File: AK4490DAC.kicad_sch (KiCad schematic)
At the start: 77 parts, among them IC1 LP5907MFX-3.3/NOPB, IC2 LP5907MFX-3.3/NOPB, IC3 LP5907MFX-3.3/NOPB, IC4 TPS7A2050PDBVR, IC5 MUSES8920, IC6 MUSES8920, IC7 MUSES8920, IC8 TPS7A2050PDBVR, IC9 AMS1117, J1 JST_XA_B02B-XASK-1, J2 USB_B_Micro, J3 SPDIF_IN, J4 LINE_OUT_L, J5 LINE_OUT_R, T1 DA103C, U1 SN74LS06NSR, U2 PCM2704CDBR, U3 TCM809TENB713, U4 TCM809TENB713, U5 AK4118, U6 AK4490, Y1 11.2896MHz, Y2 12MHz

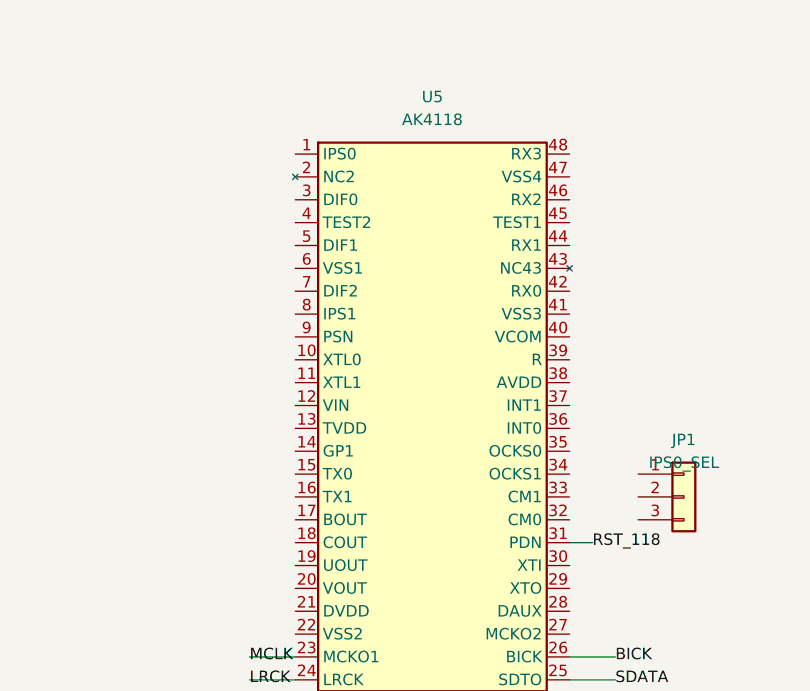
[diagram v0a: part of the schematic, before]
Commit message: Wire AK4118's static mode-select pins per verified datasheet tables
Wires 17 previously-placed-but-unconnected AK4118 pins using the same
local-label style already used for the I2S links and reset ICs, based
on the datasheet tables read in the previous commit:

  DIF2=H, DIF1=L, DIF0=H  -> Table 15 Mode 5 (24bit I2S, matches the
                             existing BICK/LRCK/SDATA/MCLK wiring)
  IPS1=L                  -> fixed; RX0/RX1 select stays on IPS0 (JP1)
  PSN=H                   -> Parallel Control Mode (this hardware-
                             pin-strap design, not I2C/SPI control)
  XTL0=L, XTL1=L          -> Table 4, matches the installed 11.2896MHz
                             crystal (Y1)
  CM1=L, CM0=L            -> Table 3 Mode 0: PLL locked to the
                             recovered SPDIF clock, SDTO=RX (the
                             correct mode for an SPDIF receiver)
  OCKS1=L, OCKS0=L        -> Table 1 default: 256fs MCLK, fs up to
                             96kHz -- the safe/universal choice; 192kHz
                             support would need OCKS1=OCKS0=H (128fs)
                             AND a matching AK4490 clock-mode change,
                             left as a follow-up decision
  VIN=L                   -> unused (no TX/DAUX passthrough in this
                             design)
  GP1=L (pin14)           -> no function in Parallel Mode; datasheet
                             Note 1 says unused inputs must not float
  NC2, NC43 tied to GND   -> "No internal bonding" pins the datasheet
                             still recommends tying to VSS3; changed
                             their pin type from no_connect to passive
                             first (no_connect flagged a new
                             no_connect_connected ERC violation when
                             wired, caught and fixed same commit)
  TEST1 (pin45) -> GND    -> datasheet: "should be connected to VSS3"

All connections reuse the GND / 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
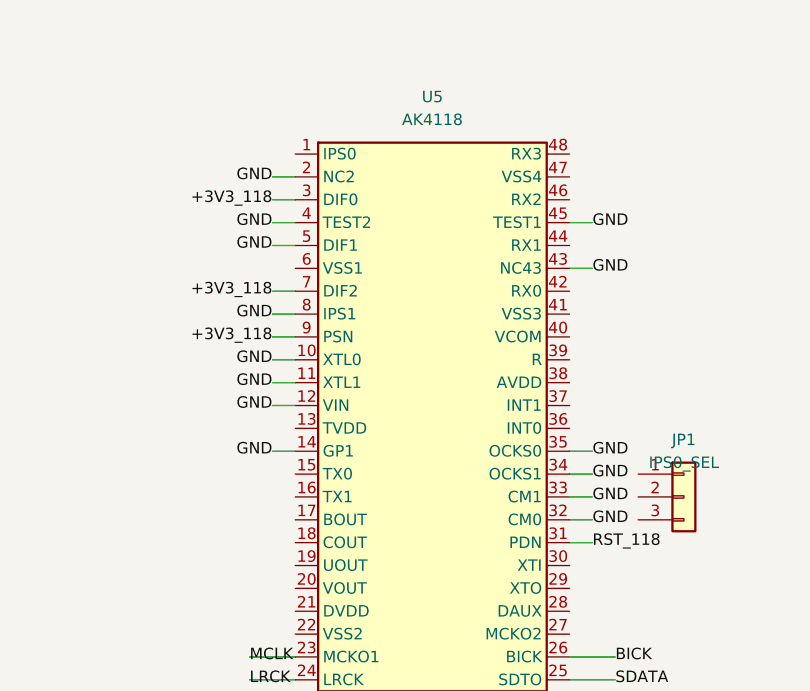
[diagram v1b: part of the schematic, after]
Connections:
- net +3V3_118: now also U5.3 (DIF0), U5.7 (DIF2), U5.9 (PSN)
- net GND: now also U5.10 (XTL0), U5.11 (XTL1), U5.12 (VIN), U5.14 (GP1), U5.2 (NC2), U5.32 (CM0), U5.33 (CM1), U5.34 (OCKS1), U5.35 (OCKS0), U5.4 (TEST2), U5.43 (NC43), U5.45 (TEST1), U5.5 (DIF1), U5.8 (IPS1)

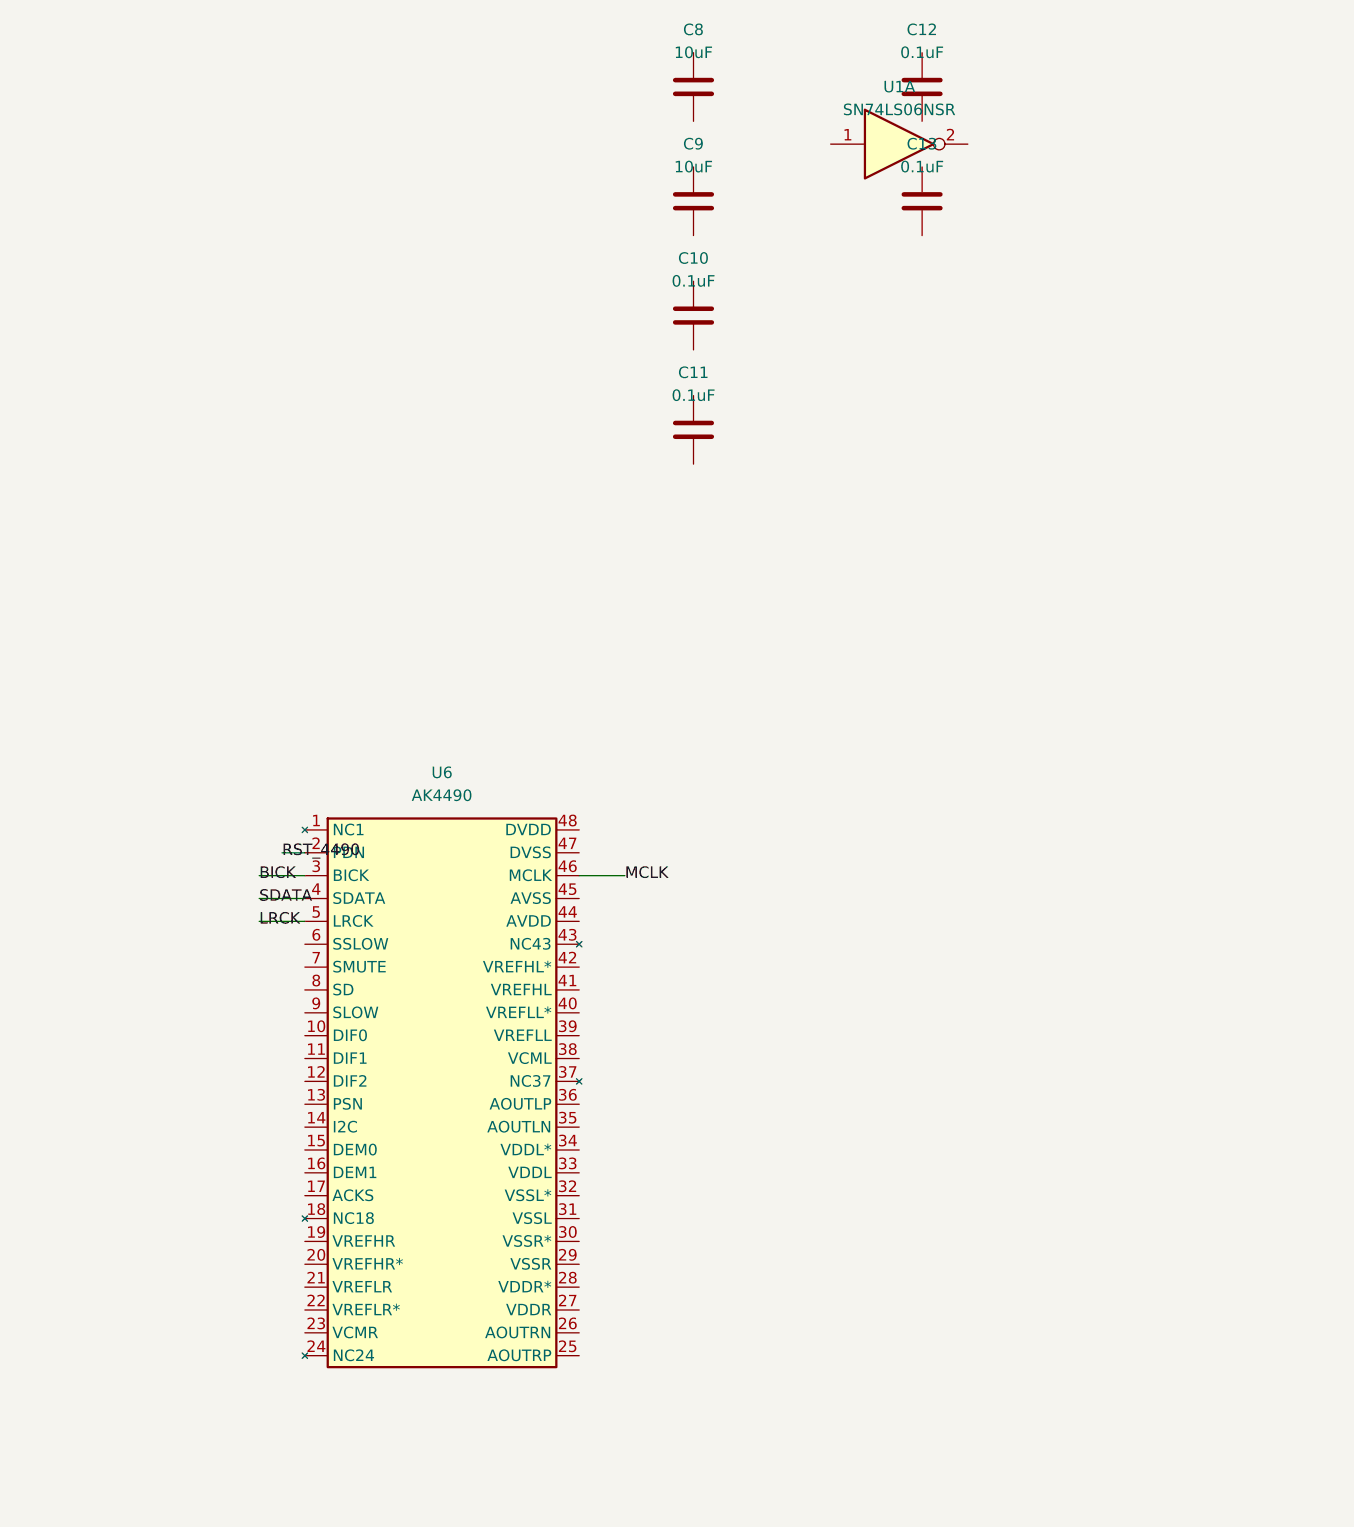
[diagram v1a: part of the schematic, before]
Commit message: Wire AK4490's static mode-select pins + VREF bias network
Verified AK4490 against the real AKM datasheet (MS1648-E-03). Good
news first: unlike AK4118, the AK4490 symbol's pin NUMBERING/NAMES
from the earlier fix (4d609bf) were already fully correct against the
real Pin Layout/Pin Functions tables (pages 5-7) -- no renaming needed
here, just wiring the mode pins to their correct levels:

  SSLOW=L, SMUTE=L          -> normal operation, mute released
  SD=H, SLOW=L              -> Table 8: Short delay Sharp roll-off
                               filter (the datasheet's own default)
  DIF2=L, DIF1=H, DIF0=H    -> Table 20 Mode 3: 24bit I2S compatible,
                               matching AK4118's I2S output (already
                               wired) and BICK>=48fs requirement
  PSN=H                     -> Parallel Control Mode (matches AK4118)
  I2C=L                     -> unused in Parallel mode (datasheet's
                               own "Handling of Unused Pin" table)
  DEM0=H, DEM1=L            -> Table 23: de-emphasis OFF (also matches
                               the same unused-pin table's required
                               setting for Parallel/PCM mode)
  ACKS=H                    -> Auto Setting Mode: MCLK/fs auto-detected
                               rather than fixed, needed because
                               AK4118's recovered MCLK frequency scales
                               with whatever sample rate the connected
                               SPDIF source actually sends
  NC pins (1,18,24,37,43) tied to GND per "No internal bonding, connect
    to GND" notes -- same no_connect-type-mismatch pattern as AK4118's
    NC2/NC43 fix last commit, fixed the same way (type -> passive)
    before wiring.

New finding (Recommended External Circuits, Fig.38): VREFHR/VREFHR*
and VREFHL/VREFHL* need a 0.1uF cap to AVDD each (bias network setting
the analog output range), and VREFLR/VREFLR*, VREFLL/VREFLL* need a
direct tie to GND -- this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
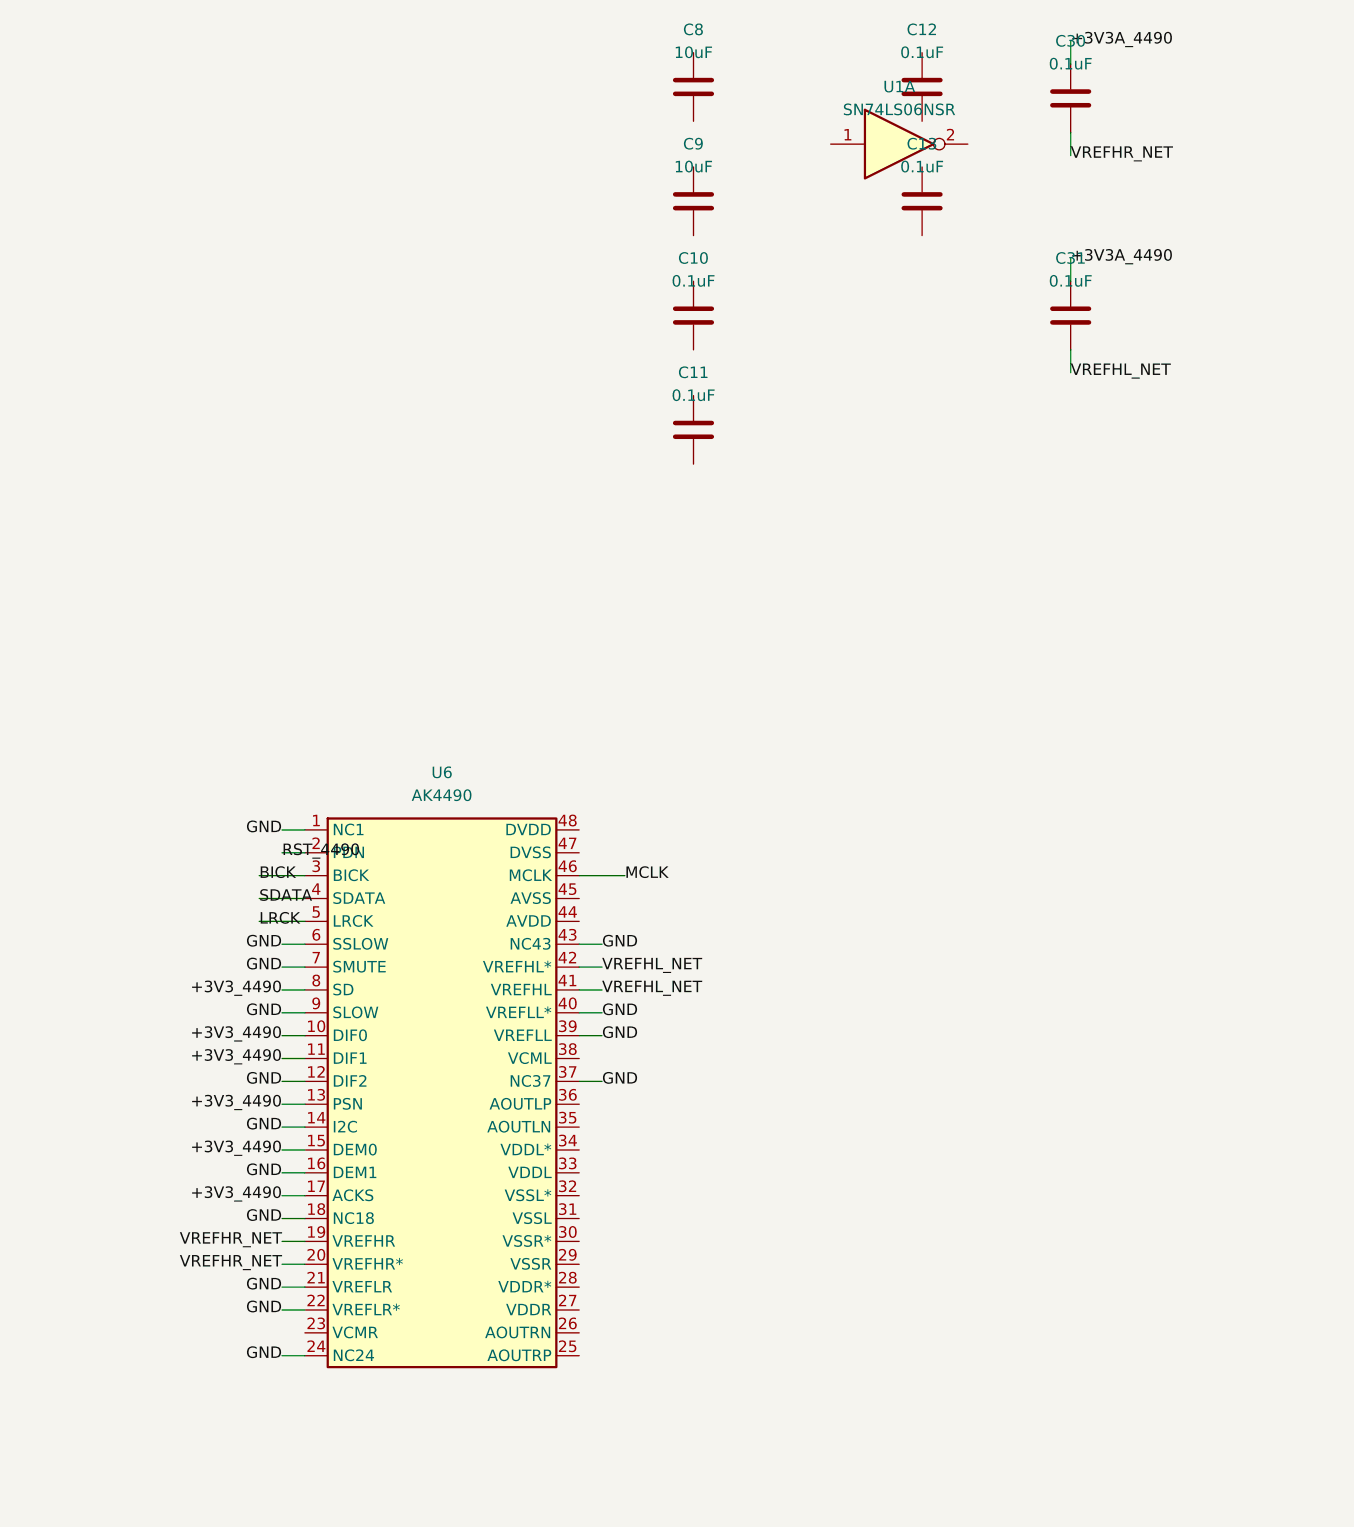
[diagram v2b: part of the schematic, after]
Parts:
- added C30, C31: 0.1uF, Capacitor_SMD:C_0603_1608Metric, symbol Device:C
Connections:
- net +3V3_4490: now also U6.10 (DIF0), U6.11 (DIF1), U6.13 (PSN), U6.15 (DEM0), U6.17 (ACKS), U6.8 (SD)
- net GND: now also U6.1 (NC1), U6.12 (DIF2), U6.14 (I2C), U6.16 (DEM1), U6.18 (NC18), U6.21 (VREFLR), U6.22 (VREFLR*), U6.24 (NC24), U6.37 (NC37), U6.39 (VREFLL), U6.40 (VREFLL*), U6.43 (NC43), U6.6 (SSLOW), U6.7 (SMUTE), U6.9 (SLOW)
- net VREFHR_NET: now reaches U6.19 (VREFHR)
- net VREFHR_NET: now also U6.20 (VREFHR*), C30.2
- net VREFHL_NET: now reaches U6.41 (VREFHL)
- net VREFHL_NET: now also U6.42 (VREFHL*), C31.2
- new net +3V3A_4490: C30.1, C31.1

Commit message: Add isolated +-15V supply (MCWI03-12D15) for output op-amp stage; fix missing op-amp units
Per discussion: the output stage needs a true bipolar +-15V supply to
match AKM's own reference circuits (Fig.40/41), and the user asked to
reuse the same isolated DC-DC approach as the original NEWDAC Eagle
design rather than build a virtual-ground single-supply version.

Confirmed by reading NEWDAC.sch (Eagle XML): the original design used
a MinMax MCWI03 series module (net "15V", same net feeding both this
module and the LM1117 3.3V/5V regulators). Datasheet confirms the
12V-input-family variant (MCWI03-12D15, accepts 4.5-18V in, +-15V out)
matches: our main DC input works directly as input, no pre-regulation
needed for this module specifically.

Added:
- U7: MCWI03-12D15 (new custom symbol -- no exact footprint match in
  KiCad's libraries, footprint left blank with a note: needs a custom
  SIP-8 THT footprint, 21.8x9.3mm body, 2.54mm pitch, before fab)
  wired: +Vin/-Vin from the main DC input (+VIN_RAW/GND, also newly
  labeled at J1 for this purpose), CON tied low (always enabled per
  datasheet: "Converter On: under 0.6VDC or open circuit"), +Vout/
  Common/-Vout -> +15V/GND/-15V (Common tied to main analog GND, i.e.
  switching-noise isolation only, not a floating ground domain like
  the USB/PCM2704C side)

Also fixed a real pre-existing bug found while working on this: IC5/
IC6/IC7 (MUSES8920, TL072 footprint) only ever had their unit-1
sub-symbol (op-amp A, pins 1/2/3) placed on the schematic -- unit 2
(op-amp B, pins 5/6/7) and unit 3 (shared V+/V- power pins 8/4) were
never instantiated, even though pins 5/6/7/8/4 were incorrectly listed
in the unit-1 instance's pin/uuid table (harmless-looking but wrong --
those pins have no graphical placement without their own unit
instance). This is exactly the ERC's pre-existing "missing_unit"
baseline (IC5/IC6/IC7 + U1/74LS06N, unchanged since the very first
commit). Split the pin list correctly and added real unit-2/unit-3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
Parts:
- removed C22, C23, C25, C26: 100pF, Capacitor_SMD:C_0603_1608Metric, symbol Device:C
- removed C24, C27: 1uF, Capacitor_SMD:C_1206_3216Metric, symbol Device:C
- removed J4: LINE_OUT_L, symbol Connector_Generic:Conn_01x02
- removed J5: LINE_OUT_R, symbol Connector_Generic:Conn_01x02
- removed R11, R12, R17, R18: 1k, Resistor_SMD:R_0603_1608Metric, symbol Device:R
- removed R13, R14, R15, R16, R19, R20, R21, R22: 10k, Resistor_SMD:R_0603_1608Metric, symbol Device:R
- added unit 3 of IC5
- added unit 2 of IC5
- added unit 3 of IC6
- added unit 2 of IC6
- added unit 3 of IC7
- added unit 2 of IC7
- added U7: MCWI03-12D15, symbol AK4490DAC:MCWI03-12D15
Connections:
- net GND: now also J1.2 (Pin_2), U7.1 (-Vin), U7.3 (CON), U7.7 (Common)
- net +VIN_RAW: now reaches J1.1 (Pin_1)
- net +VIN_RAW: now also U7.2 (+Vin)
- new net +15V: IC5.8 (V+), IC6.8 (V+), IC7.8 (V+), U7.6 (+Vout)
- new net -15V: IC5.4 (V-), IC6.4 (V-), IC7.4 (V-), U7.8 (-Vout)
